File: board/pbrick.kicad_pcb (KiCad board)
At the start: 4 copper layers, 24 x 44 mm, 62 parts, among them J1 UJC-HP-3-SMT-TR, J2 TC2030-IDC-NL, J3 U.FL2PIN, J4 QWIIC, M0 5055680471, M1 5055680471, Q1 SSM6J507NU, Q2 SSM6J507NU, U1 MIC5219-3.3YML-TR, U2 ADP3330ARTZ-5-RL7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

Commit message: Updating board
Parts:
- moved VBUS 5.24 mm to (142.8, 130.1)
- moved C10 3.93 mm to (140.2, 127.5)
- moved R1 2.39 mm to (122.3, 131.9)
- moved D3 2.29 mm to (122.3, 130.5)
- moved C8 1.95 mm to (142.8, 126.6), turned to 90 degrees
- moved C2 1.93 mm to (125.0, 129.0), turned to 90 degrees
- moved R3 1.92 mm to (138.3, 132.8)
- moved C5 1.76 mm to (121.6, 128.1)
- moved D1 1.61 mm to (123.3, 127.8), turned to 90 degrees
- moved Q1 1.59 mm to (140.4, 130.1), turned to 270 degrees
- moved R7 0.83 mm to (135.4, 101.4), turned to 270 degrees
- moved C19 0.83 mm to (141.3, 116.7)
- moved R2 0.69 mm to (122.3, 133.1), turned to 0 degrees
- moved R5 0.63 mm to (138.1, 125.2)
- moved R4 0.63 mm to (140.2, 125.2)
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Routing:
- net VDD: track 76.0 -> 129.0 mm, vias 7 -> 8
- net 3.3V: track 91.1 -> 78.9 mm, vias 5 -> 4
- net GND: track 236.4 -> 247.1 mm, vias 8 -> 10
- net /P0.18: track 12.4 -> 21.7 mm, vias 1 -> 2
- net VBUS: track 35.1 -> 44.4 mm, vias 3 -> 4
- net Net-(C10-Pad2): track 10.5 -> 16.7 mm, vias 0 -> 2
- net /VBUS_EN_SNK: track 12.6 -> 6.85 mm, vias 2 -> 0
- net /P0.22: track 53.3 -> 57.6 mm
- net /P1.00: track 11.8 -> 15.5 mm
- net /M0_0: track 44.0 -> 40.4 mm
- net Net-(C9-Pad2): track 11.7 -> 9.77 mm
- net /SWDCLK: track 10.3 -> 8.41 mm
- net Net-(R2-Pad2): track 14.7 -> 13.2 mm
- net Net-(D2-Pad1): track 6.30 -> 4.85 mm
- net /M0_1: track 37.6 -> 36.2 mm
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
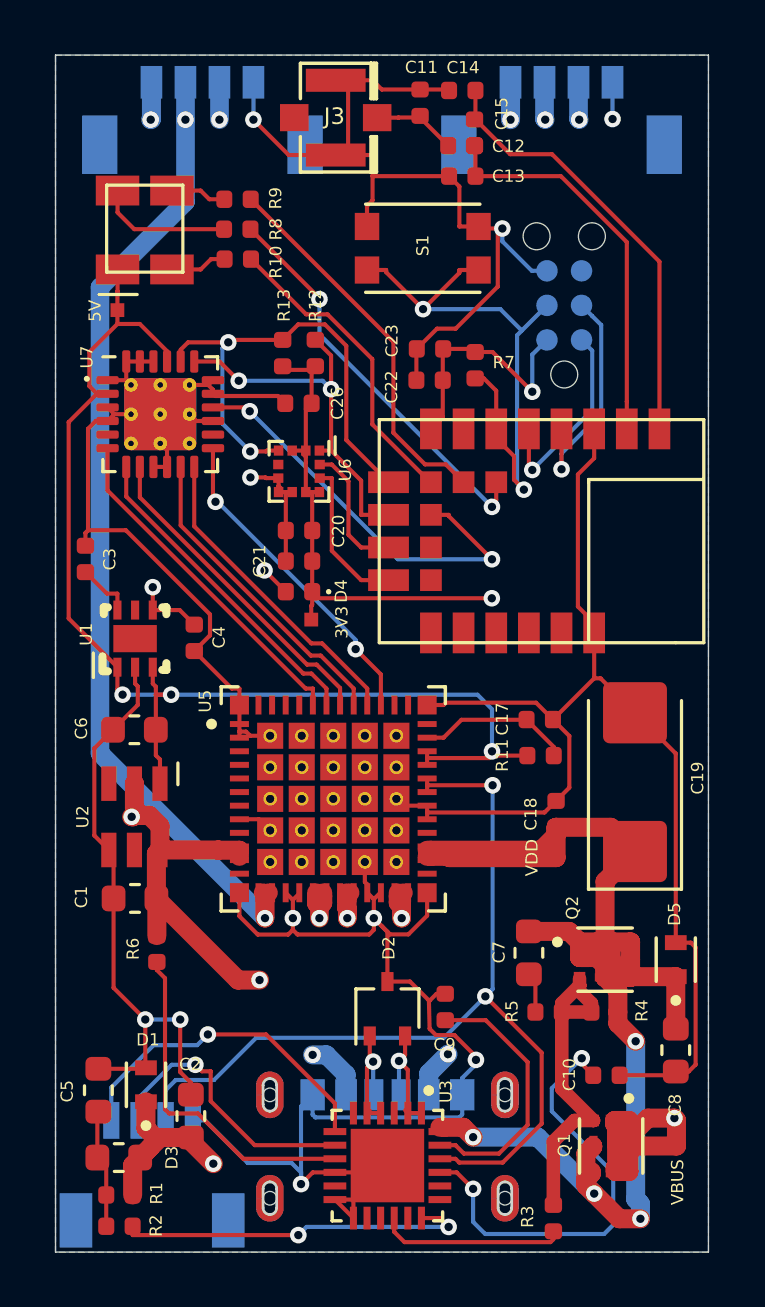
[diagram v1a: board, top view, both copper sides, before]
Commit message: Updating part list. Missing alt 12v connector
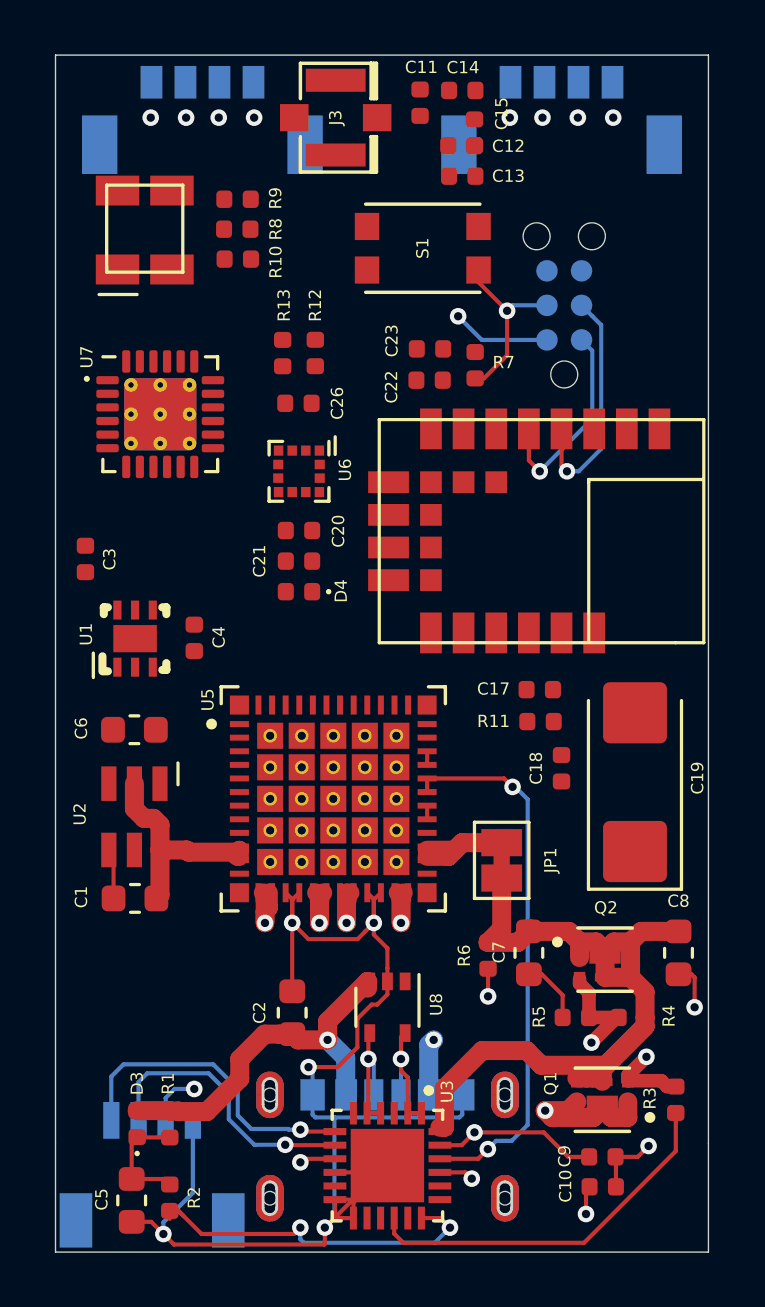
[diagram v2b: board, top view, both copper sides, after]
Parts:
- removed 3V3, 5V, VBUS, VDD: Val**, Connectors:PAD.02X.02
- removed D1, D5: ESDA25P35-1U1M, Common:TVS_ESDA25P35-1U1M
- removed D2: ESDA25W, Package_TO_SOT_SMD:SOT-323_SC-70
- added JP1: SolderJumper_2_Bridged, Jumper:SolderJumper-2_P1.3mm_Bridged_Pad1.0x1.5mm, F.Cu at (136.4, 119.6)
- added U8: ESDA25W5, Package_TO_SOT_SMD:SOT-353_SC-70-5, F.Cu at (132.2, 125.0)
- D3: footprint Resistor_SMD:R_0603_1608Metric -> Diode_SMD:D_0402_1005Metric
- moved R6 12.2 mm to (135.9, 123.1)
- moved C9 7.98 mm to (140.1, 130.5), turned to 180 degrees
- moved R3 6.26 mm to (142.8, 128.4)
- moved C2 5.32 mm to (128.7, 125.2)
- moved C5 4.23 mm to (122.8, 132.1), turned to 270 degrees
- moved C10 4.10 mm to (140.1, 131.6)
- moved C8 3.58 mm to (142.9, 123.0)
- moved R1 3.19 mm to (124.2, 129.3), turned to 90 degrees
- moved R2 2.13 mm to (124.2, 132.0), turned to 270 degrees
- moved Q1 1.73 mm to (140.1, 128.4), turned to 180 degrees
- moved C18 1.70 mm to (138.6, 116.2)
- moved D3 1.41 mm to (123.0, 129.3), turned to 90 degrees
- moved R11 1.25 mm to (137.8, 114.5)
- moved C17 1.10 mm to (137.8, 113.3)
- moved R4 1.02 mm to (141.2, 125.4)
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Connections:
- C7 pad 1: VDD -> VSS
- C8 pad 2: VDD -> VSS
- J2 pad 6: (no net) -> Net-(J2-Pad6)
- M0 pad S1: (no net) -> Net-(M0-PadS1)
- M0 pad S2: (no net) -> Net-(M0-PadS1)
- M1 pad S1: (no net) -> Net-(M1-PadS1)
- M1 pad S2: (no net) -> Net-(M1-PadS1)
- Q1 pad 4: VDD -> VSS
- Q1 pad 8: VDD -> VSS
- Q2 pad 1: VDD -> VSS
- Q2 pad 2: VDD -> VSS
- Q2 pad 4: VDD -> VSS
- Q2 pad 5: VDD -> VSS
- Q2 pad 6: VDD -> VSS
- Q2 pad 7: VDD -> VSS
- Q2 pad 8: VDD -> VSS
- R4 pad 1: VDD -> VSS
- R6 pad 1: VDD -> VSS
- U3 pad 24: VDD -> VSS
- U7 pad 25: GND -> (no net)
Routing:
- net GND: track 247.1 -> 68.2 mm, vias 10 -> 9
- net VDD: track 129.0 -> 12.7 mm, vias 8 -> 2
- net /P0.22: track 57.6 -> 11.6 mm, vias 3 -> 1
- net 5V: track 45.1 -> 0.50 mm, vias 3 -> 0
- net /P0.19: track 53.8 -> 10.4 mm, vias 3 -> 1
- net /M0_0: track 40.4 -> 2.28 mm
- net 3.3V: track 78.9 -> 42.3 mm
- net /M1_0: track 37.4 -> 2.32 mm
- net /M1_1: track 36.8 -> 2.30 mm
- net /M0_1: track 36.2 -> 2.30 mm
- net VSS: track 0.00 -> 32.6 mm
- net /ANT: track 16.2 -> 0.00 mm
- net /P1.00: track 15.5 -> 0.00 mm, vias 2 -> 0
- net /P0.18: track 21.7 -> 6.64 mm, vias 2 -> 1
- net /P0.09: track 14.9 -> 0.00 mm, vias 2 -> 0
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- removed copper zone on B.Cu, net GND
- removed copper zone on GND, net GND
- removed copper zone on M.Cu, net VBUS
- removed copper zone on M.Cu, net VDD

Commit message: Adding extra vin, manual routing
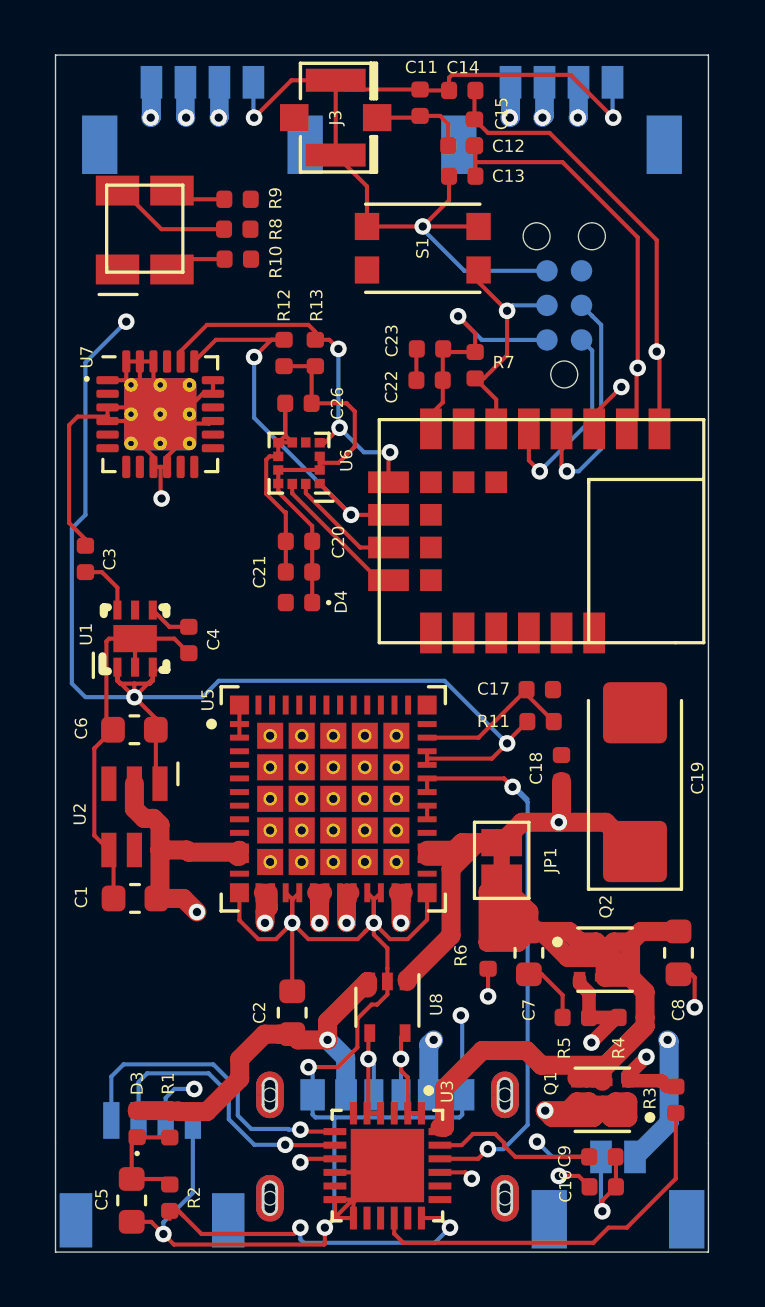
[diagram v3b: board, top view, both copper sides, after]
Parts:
- added J5: 5055670271, Common:5055670271, B.Cu at (141.3, 130.5)
- moved R13 1.20 mm to (129.6, 101.0)
- moved R12 1.15 mm to (128.4, 101.0)
- moved C20 0.40 mm to (128.9, 107.9)
- moved C21 0.40 mm to (128.9, 109.0)
- moved D4 0.40 mm to (128.9, 110.1)
- moved U6 0.30 mm to (128.9, 105.0), turned to 180 degrees
- moved C4 0.22 mm to (124.9, 111.5)
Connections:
- M0 pad S1: Net-(M0-PadS1) -> (no net)
- M0 pad S2: Net-(M0-PadS1) -> (no net)
- M1 pad S1: Net-(M1-PadS1) -> (no net)
- M1 pad S2: Net-(M1-PadS1) -> (no net)
- U1 pad GND: (no net) -> GND
- U7 pad 25: (no net) -> GND
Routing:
- net GND: track 68.2 -> 178.1 mm, vias 9 -> 14
- net VDD: track 12.7 -> 109.6 mm, vias 2 -> 5
- net 5V: track 0.50 -> 45.8 mm, vias 0 -> 3
- net /M0_0: track 2.28 -> 41.2 mm
- net /M1_1: track 2.30 -> 37.0 mm
- net /M0_1: track 2.30 -> 36.2 mm
- net /M1_0: track 2.32 -> 35.3 mm
- net 3.3V: track 42.3 -> 63.8 mm
- net /ANT: track 0.00 -> 16.6 mm, vias 0 -> 1
- net /RF: track 0.00 -> 15.5 mm, vias 0 -> 1
- net /P0.22: track 11.6 -> 26.9 mm, vias 1 -> 3
- net /P0.19: track 10.4 -> 24.8 mm, vias 1 -> 4
- net VSS: track 32.6 -> 44.7 mm
- net Net-(C17-Pad2): track 0.00 -> 5.97 mm
- net /P0.01: track 0.00 -> 5.21 mm
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- added copper zone on GND, net GND

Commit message: Unfillfing zones
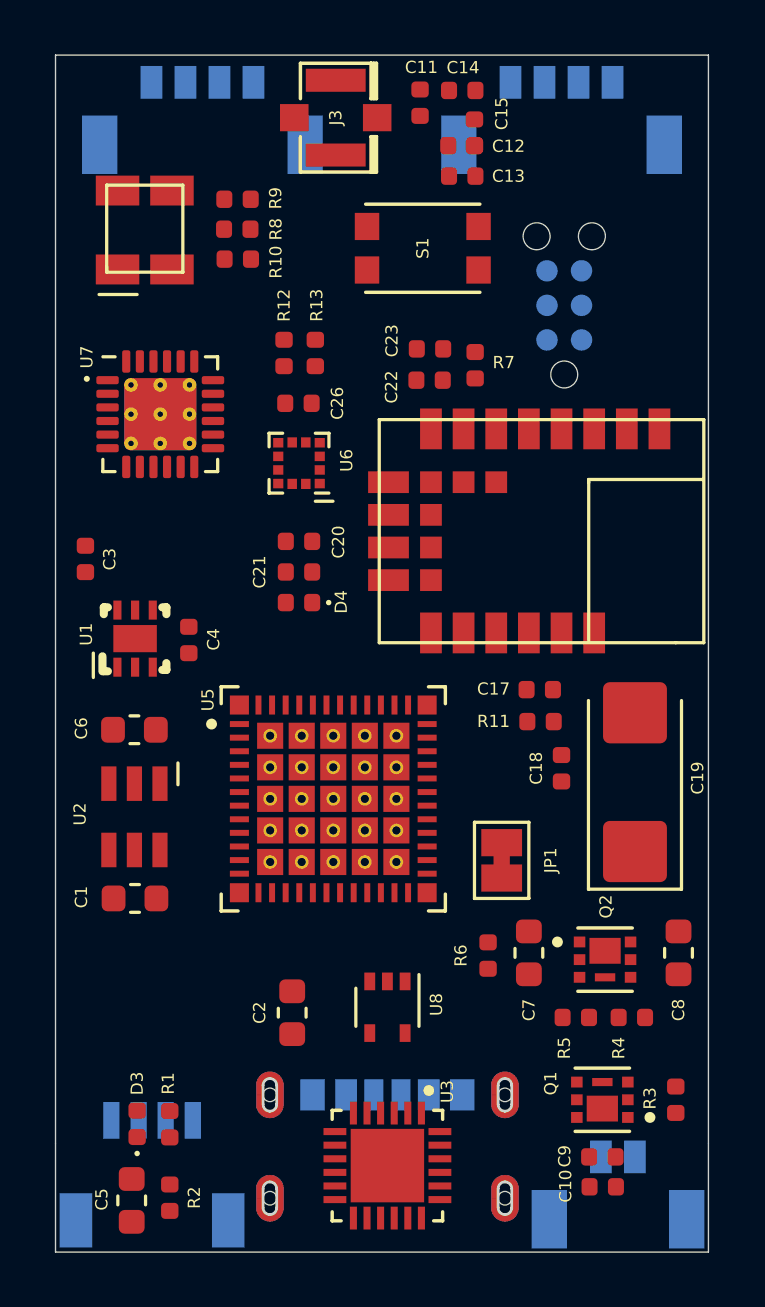
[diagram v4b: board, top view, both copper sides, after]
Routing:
- net GND: track 178.1 -> 0.00 mm, vias 14 -> 0
- net VDD: track 109.6 -> 0.00 mm, vias 5 -> 0
- net 3.3V: track 63.8 -> 0.00 mm, vias 4 -> 0
- net 5V: track 45.8 -> 0.00 mm, vias 3 -> 0
- net VSS: track 44.7 -> 0.00 mm
- net /M0_0: track 41.2 -> 0.00 mm, vias 2 -> 0
- net /M1_1: track 37.0 -> 0.00 mm, vias 2 -> 0
- net /M0_1: track 36.2 -> 0.00 mm, vias 2 -> 0
- net /M1_0: track 35.3 -> 0.00 mm, vias 2 -> 0
- net VBUS: track 34.2 -> 0.00 mm, vias 3 -> 0
- net /P0.22: track 26.9 -> 0.00 mm, vias 3 -> 0
- net /P0.19: track 24.8 -> 0.00 mm, vias 4 -> 0
- net /ANT: track 16.6 -> 0.00 mm, vias 1 -> 0
- net /RF: track 15.5 -> 0.00 mm, vias 1 -> 0
- net /DISCH: track 14.7 -> 0.00 mm, vias 2 -> 0
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- added copper zone on M.Cu, net VBUS
- removed copper zone on GND, net GND

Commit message: New routing
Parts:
- moved C2 0.20 mm to (128.7, 125.0)
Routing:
- net GND: track 0.00 -> 277.9 mm, vias 0 -> 6
- net VDD: track 0.00 -> 115.4 mm, vias 0 -> 4
- net 3.3V: track 0.00 -> 84.9 mm, vias 0 -> 6
- net /P0.19: track 0.00 -> 52.2 mm, vias 0 -> 2
- net 5V: track 0.00 -> 47.4 mm, vias 0 -> 3
- net /P0.22: track 0.00 -> 47.4 mm, vias 0 -> 3
- net /M0_0: track 0.00 -> 40.3 mm, vias 0 -> 2
- net /M1_1: track 0.00 -> 39.3 mm, vias 0 -> 4
- net /M1_0: track 0.00 -> 37.7 mm, vias 0 -> 2
- net /M0_1: track 0.00 -> 36.2 mm, vias 0 -> 2
- net VSS: track 0.00 -> 33.1 mm
- net VBUS: track 0.00 -> 31.4 mm, vias 0 -> 3
- net /P0.18: track 0.00 -> 16.9 mm, vias 0 -> 1
- net /P0.09: track 0.00 -> 16.0 mm, vias 0 -> 3
- net /ANT: track 0.00 -> 15.9 mm
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- removed copper zone on M.Cu, net VBUS

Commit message: Updating PCB
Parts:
- U3: footprint Common:QFN50P400X400X90-25N -> Package_DFN_QFN:QFN-24-1EP_4x4mm_P0.5mm_EP2.65x2.65mm_ThermalVias
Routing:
- net GND: track 277.9 -> 370.8 mm, vias 6 -> 7
- net 3.3V: track 84.9 -> 102.8 mm, vias 6 -> 9
- net VDD: track 115.4 -> 121.0 mm, vias 4 -> 5
- net VBUS: track 31.4 -> 33.4 mm, vias 3 -> 4
- net /P0.22: track 47.4 -> 49.4 mm
- net /DISCH: track 11.2 -> 12.0 mm
- added copper zone on B.Cu, net GND
- added copper zone on GND, net GND
- added copper zone on M.Cu, net GND
- added copper zone on M.Cu, net VBUS
- added copper zone on M.Cu, net VDD

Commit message: Updating Board, schematic, generated files
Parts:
- USB-C PD: renamed from J1
- renumbered J5 to PWR
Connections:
- U8 pad 1: VDD -> VSS
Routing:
- net VSS: track 33.1 -> 40.4 mm
- net VDD: track 121.0 -> 115.7 mm
- net GND: track 370.8 -> 376.0 mm

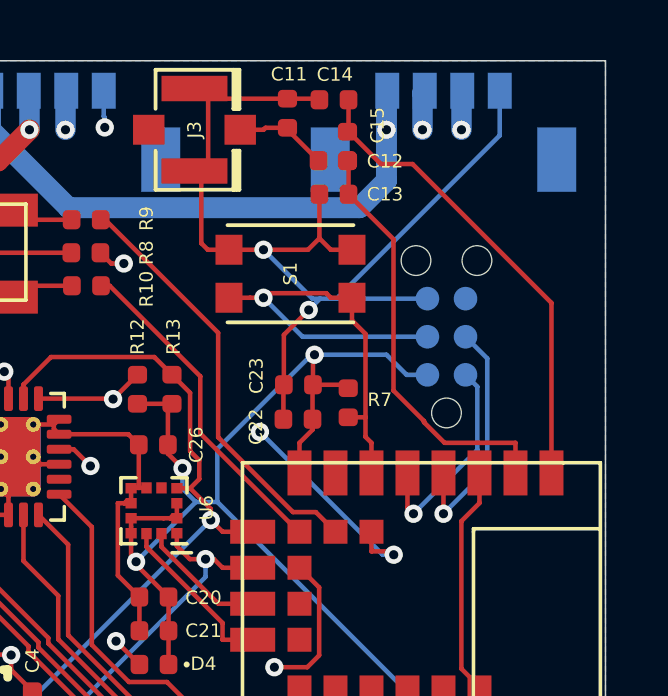
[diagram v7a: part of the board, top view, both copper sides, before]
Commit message: Minor board layout update
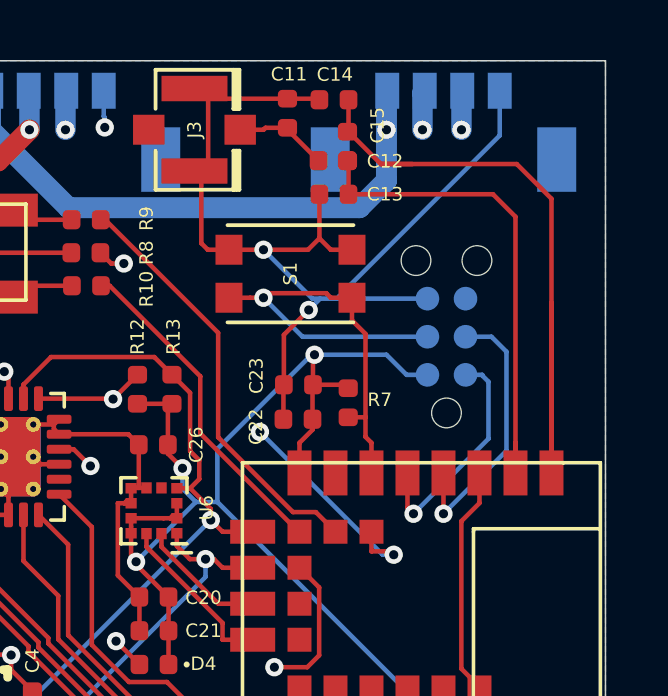
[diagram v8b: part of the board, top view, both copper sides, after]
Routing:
- net /ANT: track 15.9 -> 24.7 mm
- net /RF: track 14.1 -> 16.6 mm
- net /SWDCLK: track 8.16 -> 9.20 mm
- net /SWDIO: track 7.12 -> 7.75 mm
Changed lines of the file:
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@@
     (thickness 1.6)
     (drawings 16)
-    (tracks 961)
+    (tracks 963)
     (zones 0)
     (modules 58)
@@
   (segment (start 133.9 99.2) (end 132.6 97.9) (width 0.1524) (layer B.Cu) (net 11))
   (via (at 132.6 97.9) (size 0.6096) (layers F.Cu B.Cu) (net 11))
-  (segment (start 138.6 105.1) (end 140.059 103.641) (width 0.1524) (layer B.Cu) (net 12))
-  (segment (start 140.059 103.641) (end 140.059 99.9237) (width 0.1524) (layer B.Cu) (net 12))
-  (segment (start 140.059 99.9237) (end 139.335 99.2) (width 0.1524) (layer B.Cu) (net 12))
   (segment (start 138.6 103.74) (end 138.6 105.1) (width 0.1524) (layer F.Cu) (net 12))
   (via (at 138.6 105.1) (size 0.6096) (layers F.Cu B.Cu) (net 12))
-  (segment (start 137.6 105.1) (end 139.728 102.972) (width 0.1524) (layer B.Cu) (net 13))
-  (segment (start 139.728 102.972) (end 139.728 100.863) (width 0.1524) (layer B.Cu) (net 13))
-  (segment (start 139.728 100.863) (end 139.335 100.47) (width 0.1524) (layer B.Cu) (net 13))
+  (segment (start 138.6 105.1) (end 140.7 103) (width 0.1524) (layer B.Cu) (net 12))
+  (segment (start 140.7 103) (end 140.7 99.7) (width 0.1524) (layer B.Cu) (net 12))
+  (segment (start 140.2 99.2) (end 139.335 99.2) (width 0.1524) (layer B.Cu) (net 12))
+  (segment (start 140.7 99.7) (end 140.2 99.2) (width 0.1524) (layer B.Cu) (net 12))
   (segment (start 137.4 103.74) (end 137.4 104.9) (width 0.1524) (layer F.Cu) (net 13))
   (segment (start 137.4 104.9) (end 137.6 105.1) (width 0.1524) (layer F.Cu) (net 13))
   (via (at 137.6 105.1) (size 0.6096) (layers F.Cu B.Cu) (net 13))
+  (segment (start 137.6 105.1) (end 140.1 102.6) (width 0.1524) (layer B.Cu) (net 13))
+  (segment (start 140.1 102.6) (end 140.1 100.7) (width 0.1524) (layer B.Cu) (net 13))
+  (segment (start 140.1 100.7) (end 139.9 100.5) (width 0.1524) (layer B.Cu) (net 13))
+  (segment (start 139.891493 100.47) (end 139.335 100.47) (width 0.1524) (layer B.Cu) (net 13))
+  (segment (start 139.9 100.478507) (end 139.891493 100.47) (width 0.1524) (layer B.Cu) (net 13))
+  (segment (start 139.9 100.5) (end 139.9 100.478507) (width 0.1524) (layer B.Cu) (net 13))
   (segment (start 133.8 105.7) (end 133.7716 105.7) (width 0.1524) (layer F.Cu) (net 14))
   (segment (start 133.7716 105.7) (end 130.4932 102.4216) (width 0.1524) (layer F.Cu) (net 14))
@@
   (segment (start 135.405 93.33) (end 135.4 93.335) (width 0.1524) (layer F.Cu) (net 17))
   (segment (start 141 103.74) (end 141 102.7357) (width 0.1524) (layer F.Cu) (net 17))
-  (segment (start 135.435 94.45) (end 136.9342 95.9492) (width 0.1524) (layer F.Cu) (net 17))
-  (segment (start 136.9342 95.9492) (end 136.9342 100.9939) (width 0.1524) (layer F.Cu) (net 17))
-  (segment (start 136.9342 100.9939) (end 137.9501 102.0098) (width 0.1524) (layer F.Cu) (net 17))
-  (segment (start 137.9501 102.0098) (end 137.9502 102.0098) (width 0.1524) (layer F.Cu) (net 17))
-  (segment (start 137.9502 102.0098) (end 137.9502 102.0506) (width 0.1524) (layer F.Cu) (net 17))
-  (segment (start 137.9502 102.0506) (end 138.6353 102.7357) (width 0.1524) (layer F.Cu) (net 17))
-  (segment (start 138.6353 102.7357) (end 141 102.7357) (width 0.1524) (layer F.Cu) (net 17))
+  (segment (start 135.435 94.45) (end 140.25 94.45) (width 0.1524) (layer F.Cu) (net 17))
+  (segment (start 141 95.2) (end 141 103.74) (width 0.1524) (layer F.Cu) (net 17))
+  (segment (start 140.25 94.45) (end 141 95.2) (width 0.1524) (layer F.Cu) (net 17))
   (segment (start 135.435 92.365) (end 135.435 91.3) (width 0.1524) (layer F.Cu) (net 18))
   (segment (start 142.2 103.74) (end 142.2 98.0722) (width 0.1524) (layer F.Cu) (net 18))
-  (segment (start 142.2 98.0722) (end 137.571 93.4432) (width 0.1524) (layer F.Cu) (net 18))
-  (segment (start 137.571 93.4432) (end 136.5132 93.4432) (width 0.1524) (layer F.Cu) (net 18))
   (segment (start 136.5132 93.4432) (end 135.435 92.365) (width 0.1524) (layer F.Cu) (net 18))
   (segment (start 135.435 92.365) (end 135.4 92.365) (width 0.1524) (layer F.Cu) (net 18))
+  (segment (start 142.2 103.74) (end 142.2 94.6) (width 0.1524) (layer F.Cu) (net 18))
+  (segment (start 137.571 93.4432) (end 136.5132 93.4432) (width 0.1524) (layer F.Cu) (net 18))
+  (segment (start 141.0432 93.4432) (end 142.2 94.6) (width 0.1524) (layer F.Cu) (net 18))
+  (segment (start 136.5132 93.4432) (end 141.0432 93.4432) (width 0.1524) (layer F.Cu) (net 18))
   (segment (start 122.275 110.4) (end 122.275 109.7957) (width 0.1524) (layer F.Cu) (net 19))
   (segment (start 121.1 109.006) (end 121.8897 109.7957) (width 0.1524) (layer F.Cu) (net 19))
